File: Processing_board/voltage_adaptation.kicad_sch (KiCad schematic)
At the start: 20 parts, among them J8 Conn_01x03_Pin, J9 Conn_01x03_Pin, Q1 DMP3056LSS-13, U5 LD1117S50TR_SOT223, U6 LD1117S33TR_SOT223, U7 LD1117DT18TR

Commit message: added Block Diagram (in KiCad and PDF) ; minor silkscreen cleanup
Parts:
- C28, C30, C32: Link https://www.mouser.ch/ProductDetail/Samsung-Electro-Mechani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 -> https://eu.mouser.com/ProductDetail/Samsung-Electro-Mechani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; Manufacturer_Part_Number CL05B104KP5VPNC -> CL05B104KP5VPNC
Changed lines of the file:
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@@
 			)
 		)
-		(property "Link" "https://www.mouser.ch/ProductDetail/Samsung-Electro-Mechanics/CL05B104KP5VPNC?qs=gqBM4hNBiUXTv%252BkFO9q2pQ%3D%3D"
+		(property "Link" "https://eu.mouser.com/ProductDetail/Samsung-Electro-Mechanics/CL05B104KP5VPNC?qs=gqBM4hNBiUXTv%252BkFO9q2pQ%3D%3D"
 			(at 53.34 120.65 0)
 			(effects
@@
 			)
 		)
-		(property "Manufacturer_Part_Number" "CL05B104KP5VPNC"
+		(property "Manufacturer_Part_Number" "CL05B104KP5VPNC "
 			(at 53.34 120.65 0)
 			(effects
@@
 			)
 		)
-		(property "Link" "https://www.mouser.ch/ProductDetail/Samsung-Electro-Mechanics/CL05B104KP5VPNC?qs=gqBM4hNBiUXTv%252BkFO9q2pQ%3D%3D"
+		(property "Link" "https://eu.mouser.com/ProductDetail/Samsung-Electro-Mechanics/CL05B104KP5VPNC?qs=gqBM4hNBiUXTv%252BkFO9q2pQ%3D%3D"
 			(at 194.31 118.11 0)
 			(effects
@@
 			)
 		)
-		(property "Manufacturer_Part_Number" "CL05B104KP5VPNC"
+		(property "Manufacturer_Part_Number" "CL05B104KP5VPNC "
 			(at 194.31 118.11 0)
 			(effects
@@
 			)
 		)
-		(property "Link" "https://www.mouser.ch/ProductDetail/Samsung-Electro-Mechanics/CL05B104KP5VPNC?qs=gqBM4hNBiUXTv%252BkFO9q2pQ%3D%3D"
+		(property "Link" "https://eu.mouser.com/ProductDetail/Samsung-Electro-Mechanics/CL05B104KP5VPNC?qs=gqBM4hNBiUXTv%252BkFO9q2pQ%3D%3D"
 			(at 240.03 119.38 0)
 			(effects
@@
 			)
 		)
-		(property "Manufacturer_Part_Number" "CL05B104KP5VPNC"
+		(property "Manufacturer_Part_Number" "CL05B104KP5VPNC "
 			(at 240.03 119.38 0)
 			(effects

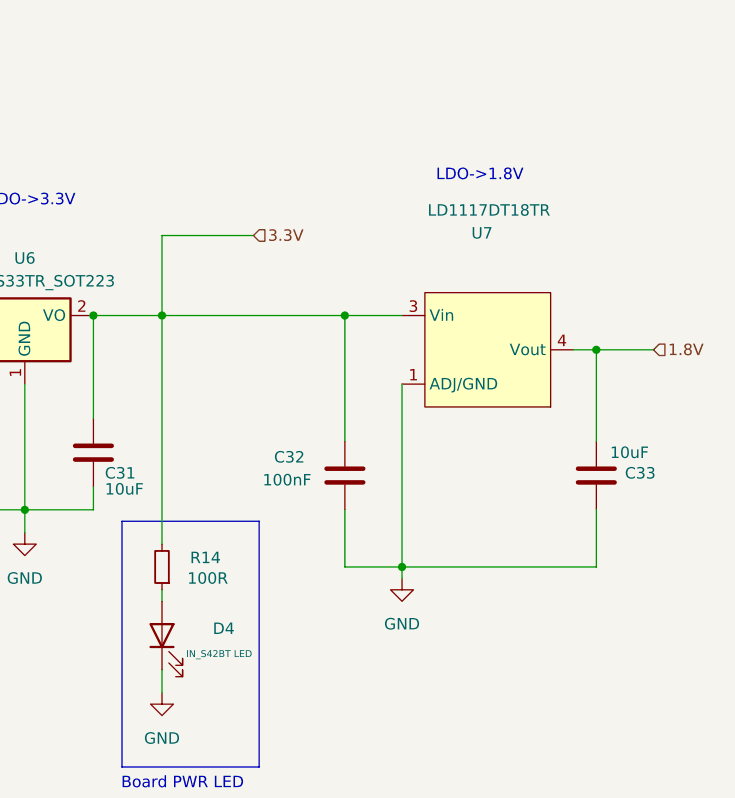
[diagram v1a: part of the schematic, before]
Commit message: Add the footprint for ADC components
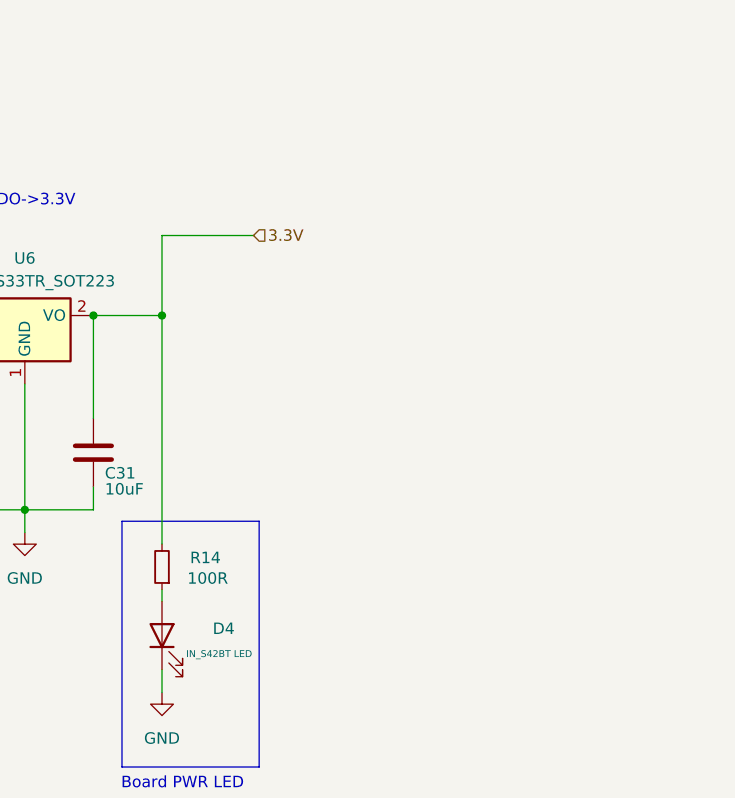
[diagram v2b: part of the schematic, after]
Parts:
- removed C32: 100nF, Capacitor_SMD:C_0402_1005Metric, symbol Device:C
- removed C33: 10uF, Capacitor_SMD:C_0402_1005Metric, symbol Device:C
- removed U7: LD1117DT18TR, LD1117DT18TR:TO228P972X240-3N, symbol Custom_Symbol_Library_Npulse:LD1117DT18TR
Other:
- note removed: "LDO->1.8V"

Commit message: feat: finalized ADC design
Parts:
- C28, C29, C30, C31: footprint Capacitor_SMD:C_0402_1005Metric -> Capacitor_SMD:C_0201_0603Metric_Pad0.64x0.40mm_HandSolder
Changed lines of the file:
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@@
 			)
 		)
-		(property "Footprint" "Capacitor_SMD:C_0402_1005Metric"
+		(property "Footprint" "Capacitor_SMD:C_0201_0603Metric_Pad0.64x0.40mm_HandSolder"
 			(at 52.3748 116.84 0)
 			(effects
@@
 			)
 		)
-		(property "Footprint" "Capacitor_SMD:C_0402_1005Metric"
+		(property "Footprint" "Capacitor_SMD:C_0201_0603Metric_Pad0.64x0.40mm_HandSolder"
 			(at 80.3148 116.84 0)
 			(effects
@@
 			)
 		)
-		(property "Footprint" "Capacitor_SMD:C_0402_1005Metric"
+		(property "Footprint" "Capacitor_SMD:C_0201_0603Metric_Pad0.64x0.40mm_HandSolder"
 			(at 195.2752 121.92 0)
 			(effects
@@
 			)
 		)
-		(property "Footprint" "Capacitor_SMD:C_0402_1005Metric"
+		(property "Footprint" "Capacitor_SMD:C_0201_0603Metric_Pad0.64x0.40mm_HandSolder"
 			(at 213.0552 120.65 0)
 			(effects
